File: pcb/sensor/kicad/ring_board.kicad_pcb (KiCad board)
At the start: 2 copper layers, 66.3 x 125.8 mm, 11 parts, among them J1 5V in (FFC), J2 CN2 mate (TBD), J3 mic carrier, U1 SHT45

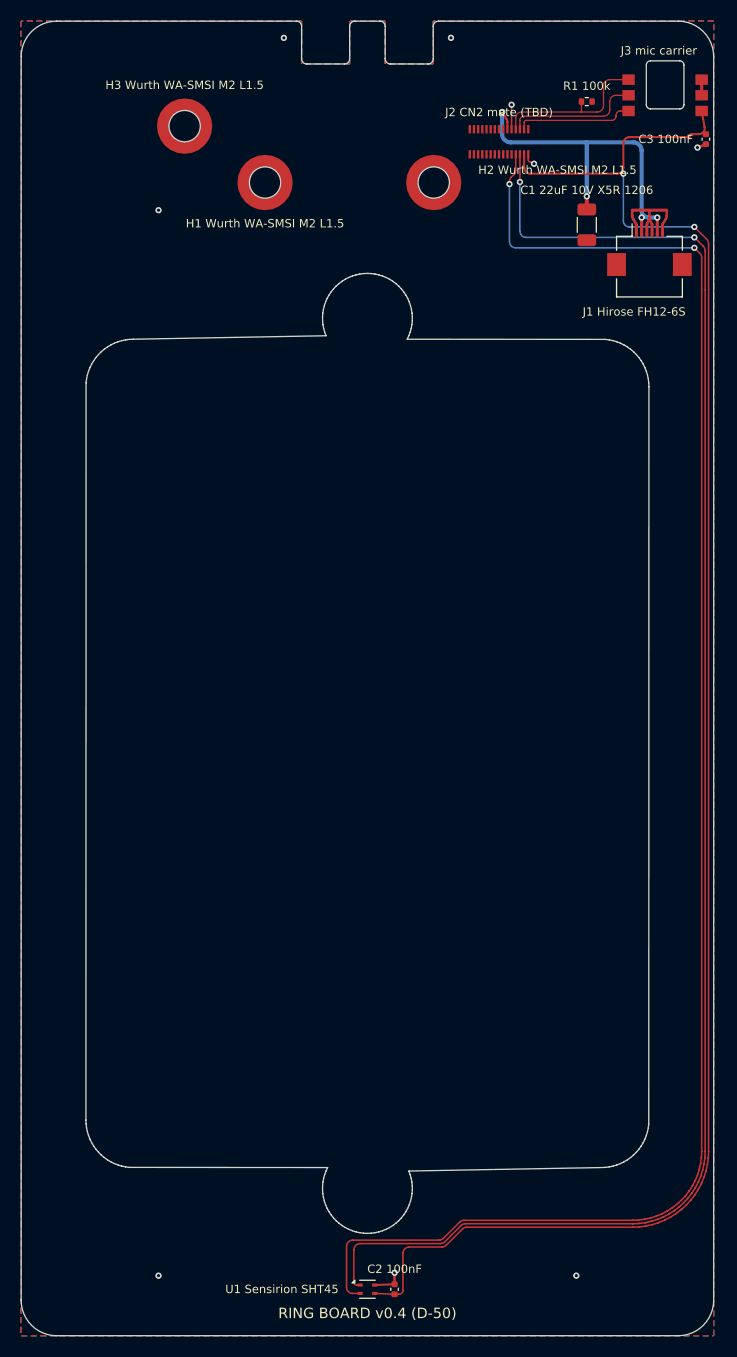
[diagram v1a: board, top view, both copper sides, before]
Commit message: Mic on the boards, parts audit, rocker second source, CN2 land pattern, back cover fit (D-82..D-90)
- Prototype PCBWay packs for the ring board, EU cap board and cover flex; logos and URL on the
  boards with room for them
- CN2 mate: Molex 55909-2474 on an assumed 51338-2474 (D-82); land pattern from Molex
  SD-55909-003 rev J, B2B from SD-51338-003 rev K (D-89); contact map and pin 1 still open
- Microphone: Knowles SPK0641HT4H-1 + ADAU7002 on the ring board and the EU cap board, the mic
  carrier removed; face plate sound column on a gasket (D-83); C3 KEMET C1206C104J3GACTU C0G
  (D-85)
- Parts rule (active, stocked at DigiKey or Mouser) and audit: F1 3403.0166.11, cover flex 1 uF
  CL05A105KO5NNNC, rocker at Mouser 979-1802.2504 (D-84)
- Rocker: tabs soldered into plated slots accepted (D-86); E-Switch RA412C1100 second source,
  slotted footprint on the wiring board and the EU mains board, solder the rocker after the
  board is screwed down (D-88)
- Back cover: round-over 8.1 x 8.0 from the printed gauges (D-87); four tabs inside the long
  side walls into the housing's slots (D-90); back_gauges_PLA
- make stock / make order-push (pcb/tools/distributors.py): live DigiKey / Mouser stock and
  lifecycle, DigiKey myLists link and Mouser cart; keys from the environment only
- Boards ERC / DRC clean; make check, make eu, make check-renders pass; renders, fab and
  order packs regenerated
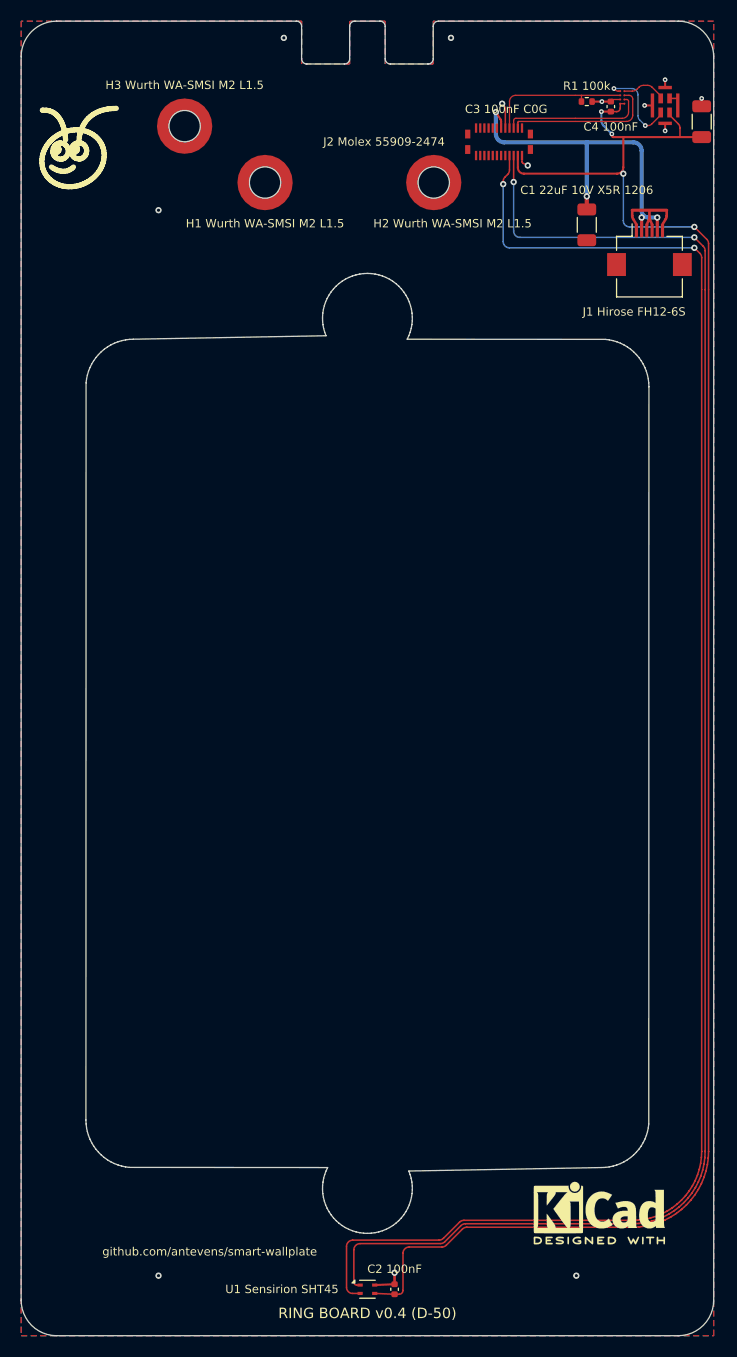
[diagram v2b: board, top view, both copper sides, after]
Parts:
- removed J3: mic carrier, sensor:Mic_Carrier_Land_2x3
- added C4: 100nF, sensor:C_0402_1005Metric, F.Cu at (123.3, 38.1)
- added LOGO1: Ant_Logo_8mm_SilkScreen, sensor:Ant_Logo_8mm_SilkScreen, F.Cu at (72.4, 42.0)
- added LOGO2: KiCad-Logo2_5mm_SilkScreen, sensor:KiCad-Logo2_5mm_SilkScreen, F.Cu at (122.2, 144.0)
- added MK1: SPK0641HT4H-1, sensor:Knowles_SPK0641HT4H-1_3x4mm, F.Cu at (128.5, 38.0)
- added U2: ADAU7002, sensor:Analog_WLCSP-8_0.76x1.56mm_P0.4mm, F.Cu at (124.4, 37.2)
- C3: value 100nF -> 100nF C0G; footprint sensor:C_0402_1005Metric -> sensor:C_1206_3216Metric
- J2: value CN2 mate (TBD) -> 55909-2474; footprint sensor:B2B_0.4mm_2x15_PLACEHOLDER -> sensor:Molex_SlimStack_55909-2474_2x12_P0.40mm_Vertical
- moved C3 1.72 mm to (132.0, 39.5), turned to 90 degrees
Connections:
- J2 pad 13: unconnected-(J2-Pin_13-Pad13) -> +5V
- J2 pad 15: unconnected-(J2-Pin_15-Pad15) -> GND
- J2 pad 17: unconnected-(J2-Pin_17-Pad17) -> /I2S_SD
- J2 pad 18: unconnected-(J2-Pin_18-Pad18) -> /SCL
- J2 pad 19: +5V -> /I2S_WS
- J2 pad 20: unconnected-(J2-Pin_20-Pad20) -> /SDA
- J2 pad 21: GND -> /I2S_SCK
- J2 pad 22: unconnected-(J2-Pin_22-Pad22) -> +3V3
- J2 pad 23: /I2S_SD -> unconnected-(J2-Pin_23-Pad23)
- J2 pad 24: /SCL -> GND
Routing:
- net /PDM_DAT: track 0.00 -> 8.61 mm, vias 0 -> 2
- net +3V3: track 165.1 -> 172.8 mm, vias 2 -> 4
- net /PDM_CLK: track 0.00 -> 4.27 mm
- net GND: track 16.4 -> 20.5 mm, vias 9 -> 13
- net /I2S_WS: track 10.9 -> 13.2 mm
- net /I2S_SD: track 15.3 -> 13.6 mm
- net /I2S_SCK: track 12.5 -> 14.0 mm
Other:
- outline, holes or cut-outs redrawn
- board text added: "C3 100nF C0G"
- board text added: "C4 100nF"
- board text added: "J2 Molex 55909-2474"
- board text added: "J2 PIN MAP AND PIN 1 ARE PLACEHOLDERS - DO NOT FABRICATE"
- board text added: "github.com/antevens/smart-wallplate"
- board text removed: "C3 100nF"
- board text removed: "J2 CN2 mate (TBD)"
- board text removed: "J2 FOOTPRINT AND PIN MAP ARE PLACEHOLDERS - DO NOT FABRICATE"
- board text removed: "J3 mic carrier"

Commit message: Parts and order lists: EU PE connector, 22 uF C1, unit and devkit lists, E-Switch rocker (D-94, D-95, D-97)
- D-94: the EU lights' PE joined in the box in a WAGO 221-412 (EXTRA_EU, ASSEMBLY step 5); the
  boards carry no PE; the steel piece's insulation added to the EU review checklist
- D-95: 22 uF C1 KEMET C1206C226M4PACTU (16 V X5R, 1.8 max) on the ring board, the EU cap board
  and the EU 5 V board; the Samsung CL31A226KPHNNNE has a 61-week maker lead time
- D-97: make order writes unit_na, unit_eu, devkit_na, devkit_eu (4 sets per variant,
  DEVKIT_SETS), exact counts; the PCBWay packs are the devkit (5 PCBs per design); the old
  3 NA + 2 EU lists removed
- Rocker: both variants' lists take the E-Switch RA412C1100 (RA4 datasheet rating option C:
  UL/cUL 10 A 250 VAC; ENEC 10(4) A 250 V~); the Marquardt stays the reference part
- ADAU7002 to DigiKey in Mouser orders (Mouser does not restock it); stale PCBWay notes fixed
- Boards ERC / DRC clean; renders regenerated
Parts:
- C1: value 22uF 10V X5R -> 22uF 16V X5R
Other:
- board text added: "C1 22uF 16V X5R 1206"
- board text removed: "C1 22uF 10V X5R 1206"

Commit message: Cost: SHT40, Murata C0G, GCT FFC (D-98)
- U1 SHT45-AD1B-R2 -> SHT40-AD1B-R2 (same SHT4x DFN-4, I2C 0x44; 9.76 -> 3.10 CAD); renamed in
  the CAD, generators and docs
- C3 KEMET C1206C104J3GACTU -> Murata GRM3195C1H104JA05D (100 nF C0G 50 V 1206, 0.95 max;
  3.52 -> 0.58)
- W1 FFC Wurth 687606152002 -> GCT 05-06-A-0152-A-4-06-4-G (same cable; 4.67 -> 3.26), the
  Wurth as the alternative
- DigiKey, one plate: NA 90.04 -> 79.03, EU 88.51 -> 78.91 CAD; boards ERC / DRC clean, order
  lists and PCBWay packs regenerated
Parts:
- U1: value SHT45 -> SHT40
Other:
- board text added: "U1 Sensirion SHT40"
- board text removed: "U1 Sensirion SHT45"

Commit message: v0.5: back cover ends, mains spacing 3.0 mm, NA fuse separation, labels, bare renders (D-101..D-106)
- D-101: back cover shell gauges (R15..R20.9); the stadium end is confirmed
- D-102: mains spacing 3.0 mm on high-CTI FR4 (MAINS_GAP, NA and EU)
- D-103: back cover end walls 1.40 mm, inside 0.2 mm longer (BC_END_WALL)
- D-104: NA wiring board: any two mains nets 3.0 mm apart, L_F re-routed
  F1.2 -> RV1.1, L_SW vias below F1, L_SW pour up towards the rocker;
  EU mains board checked, unchanged
- D-105: rocker silkscreen "E-Switch RA412C1100 or Marquardt 1802.2504",
  EU 5 V socket part on its label; bare 3D renders for every board
- D-106: version v0.5; v0.4 fab packs, PCBWay packs and renders removed
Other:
- board text added: "RING BOARD v0.5 (D-50)"
- board text removed: "RING BOARD v0.4 (D-50)"
